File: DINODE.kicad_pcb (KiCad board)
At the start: 2 copper layers, 76.2 x 90.2 mm, 35 parts, among them J1 Barrel_Jack, J10 Conn_01x03_Male, J11 Conn_02x04_Odd_Even, J12 Conn_01x03_Female, J13 Conn_02x04_Odd_Even, J2 Conn_01x02_Male, J3 Conn_01x07, J4 Conn_01x16, J5 Conn_02x04_Odd_Even, J6 Conn_02x04_Odd_Even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

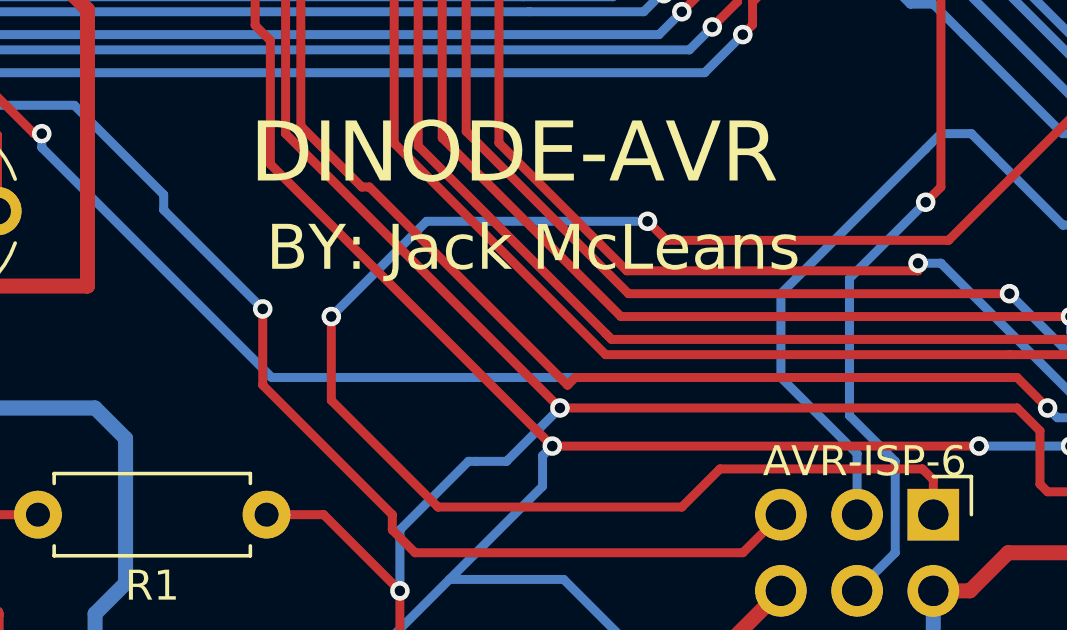
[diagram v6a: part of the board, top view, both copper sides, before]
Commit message: Addition of open-source logo
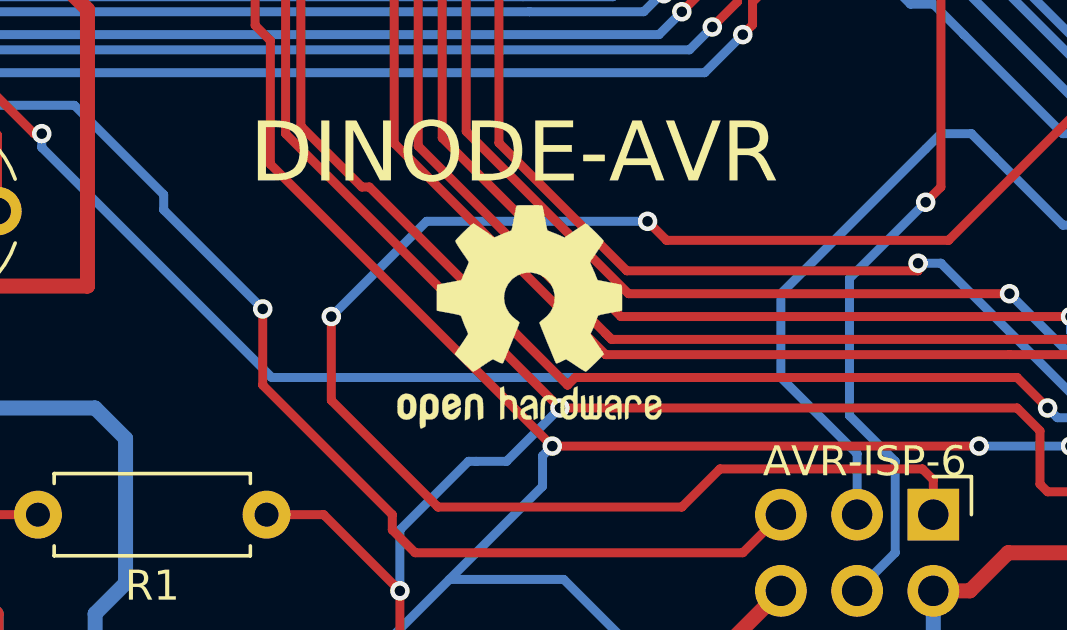
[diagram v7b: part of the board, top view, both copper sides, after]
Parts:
- added REF**: OSHW-Logo2_9.8x8mm_SilkScreen, Symbol:OSHW-Logo2_9.8x8mm_SilkScreen, F.Cu at (123.7, 107.7)
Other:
- board text added: "BY: JACK MCLEANS"
- board text removed: "BY: Jack McLeans"
